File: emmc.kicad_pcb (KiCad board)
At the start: 2 copper layers, 12.9 x 15.7 mm, 5 parts

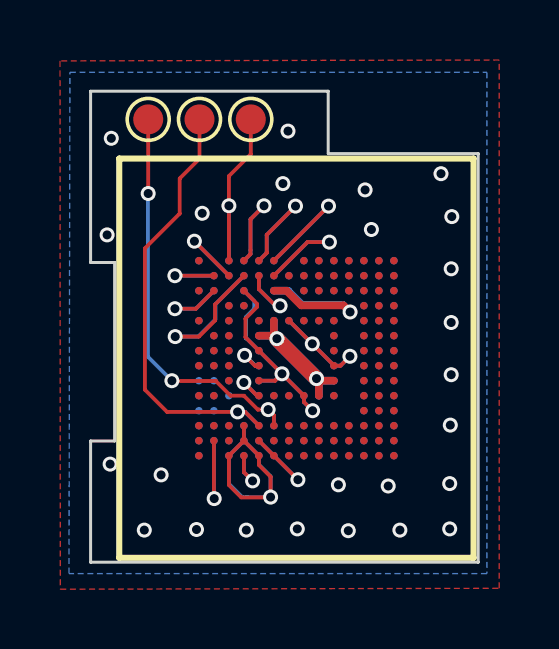
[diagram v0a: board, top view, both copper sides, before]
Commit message: Revision: * Change background plane to hatched mode. This is hopefully could reduce the 'bending' pcb, when heated. * All pin will be shown. Hopefully it will make the 'orientation alignment' worked.
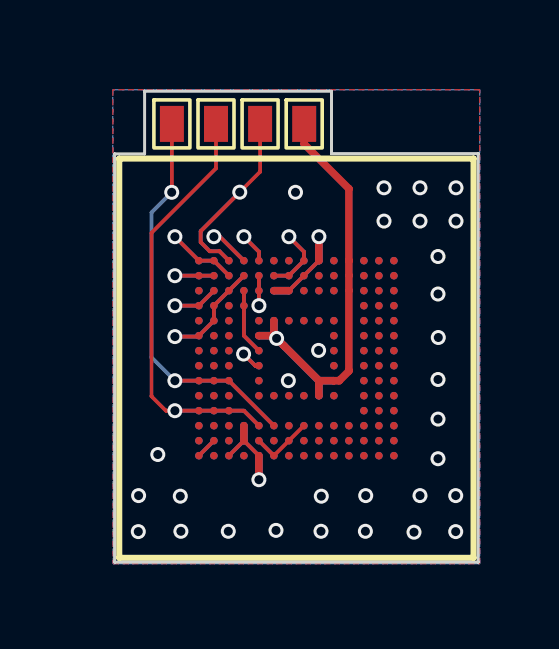
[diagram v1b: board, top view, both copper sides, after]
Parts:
- added SP4: VDDF, SniffPoint:VDDF, F.Cu at (146.9, 93.3)
- SP1: value M -> CMD
- SP2: value L -> CLK
- SP3: value A -> DAT0
- moved SP2 0.80 mm to (142.5, 93.3)
- moved SP1 0.57 mm to (144.0, 93.3)
- moved SP3 0.34 mm to (145.4, 93.3)
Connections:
- Bottom1 pad : (no net) -> Net-(Bottom1-DAT4)
- Bottom1 pad K5: Net-(Bottom1-RSTN) -> unconnected-(Bottom1-RSTN-PadK5)
- Top1 pad : (no net) -> VDDF
- Top1 pad K5: Net-(Bottom1-RSTN) -> unconnected-(Top1-RSTN-PadK5)
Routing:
- net GND: track 32.4 -> 8.73 mm, vias 33 -> 30
- net VDDF: track 8.46 -> 17.7 mm, vias 2 -> 1
- net VDD: track 17.6 -> 10.9 mm
- net Net-(Bottom1-CLK): track 13.9 -> 17.0 mm, vias 3 -> 2
- net Net-(Bottom1-DAT2): track 4.65 -> 2.01 mm
- net Net-(Bottom1-DAT0): track 6.84 -> 9.36 mm
- net Net-(Bottom1-CMD): track 15.0 -> 17.0 mm
- net Net-(Bottom1-DAT1): track 4.22 -> 2.66 mm
- net Net-(Bottom1-DAT4): track 3.25 -> 4.68 mm
- net Net-(Bottom1-RSTN): track 1.37 -> 0.00 mm, vias 1 -> 0
- net Net-(Bottom1-DAT6): track 2.77 -> 2.00 mm
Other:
- board size 12.9 x 15.7 mm -> 12.1 x 15.7 mm
